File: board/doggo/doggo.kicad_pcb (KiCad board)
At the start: 2 copper layers, 42 x 41.6 mm, 0 parts

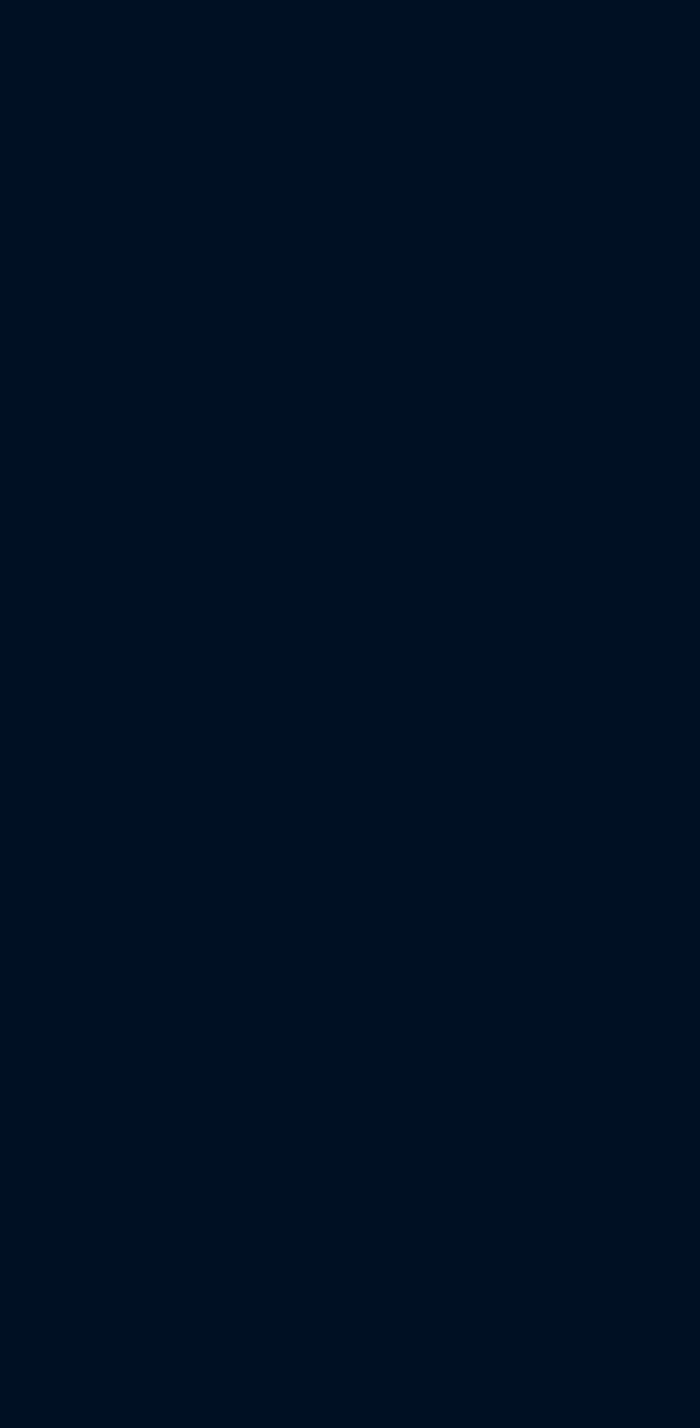
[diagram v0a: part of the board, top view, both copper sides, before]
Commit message: laying out LEDs
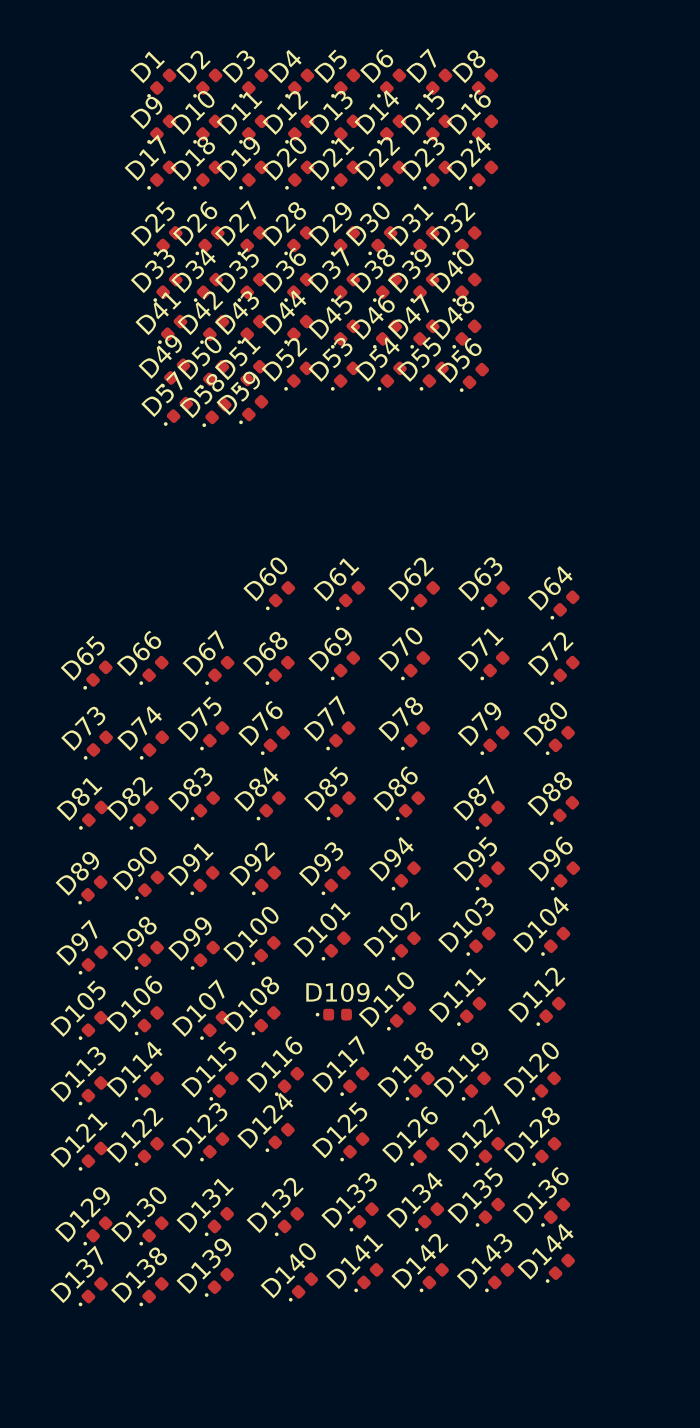
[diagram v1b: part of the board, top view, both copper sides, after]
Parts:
- added D1: LED, Diode_SMD:D_0402_1005Metric, F.Cu at (37.0, 59.0)
- added D10: LED, Diode_SMD:D_0402_1005Metric, F.Cu at (39.5, 61.5)
- added D100: LED, Diode_SMD:D_0402_1005Metric, F.Cu at (42.7, 106.2)
- added D101: LED, Diode_SMD:D_0402_1005Metric, F.Cu at (46.5, 105.9)
- added D102: LED, Diode_SMD:D_0402_1005Metric, F.Cu at (50.3, 105.9)
- added D103: LED, Diode_SMD:D_0402_1005Metric, F.Cu at (54.4, 105.7)
- added D104: LED, Diode_SMD:D_0402_1005Metric, F.Cu at (58.4, 105.7)
- added D105: LED, Diode_SMD:D_0402_1005Metric, F.Cu at (33.3, 110.2)
- added D106: LED, Diode_SMD:D_0402_1005Metric, F.Cu at (36.3, 110.0)
- added D107: LED, Diode_SMD:D_0402_1005Metric, F.Cu at (39.9, 110.2)
- added D108: LED, Diode_SMD:D_0402_1005Metric, F.Cu at (42.7, 110.0)
- added D109: LED, Diode_SMD:D_0402_1005Metric, F.Cu at (46.5, 109.7)
- added D11: LED, Diode_SMD:D_0402_1005Metric, F.Cu at (42.0, 61.5)
- added D110: LED, Diode_SMD:D_0402_1005Metric, F.Cu at (50.0, 109.7)
- added D111: LED, Diode_SMD:D_0402_1005Metric, F.Cu at (53.8, 109.5)
- added D112: LED, Diode_SMD:D_0402_1005Metric, F.Cu at (58.2, 109.5)
- added D113: LED, Diode_SMD:D_0402_1005Metric, F.Cu at (33.3, 113.8)
- added D114: LED, Diode_SMD:D_0402_1005Metric, F.Cu at (36.3, 113.5)
- added D115: LED, Diode_SMD:D_0402_1005Metric, F.Cu at (40.4, 113.5)
- added D116: LED, Diode_SMD:D_0402_1005Metric, F.Cu at (43.9, 113.3)
- added D117: LED, Diode_SMD:D_0402_1005Metric, F.Cu at (47.5, 113.3)
- added D118: LED, Diode_SMD:D_0402_1005Metric, F.Cu at (51.1, 113.5)
- added D119: LED, Diode_SMD:D_0402_1005Metric, F.Cu at (54.1, 113.5)
- added D12: LED, Diode_SMD:D_0402_1005Metric, F.Cu at (44.5, 61.5)
- added D120: LED, Diode_SMD:D_0402_1005Metric, F.Cu at (57.9, 113.5)
- added D121: LED, Diode_SMD:D_0402_1005Metric, F.Cu at (33.3, 117.3)
- added D122: LED, Diode_SMD:D_0402_1005Metric, F.Cu at (36.3, 117.1)
- added D123: LED, Diode_SMD:D_0402_1005Metric, F.Cu at (39.9, 116.8)
- added D124: LED, Diode_SMD:D_0402_1005Metric, F.Cu at (43.4, 116.3)
- added D125: LED, Diode_SMD:D_0402_1005Metric, F.Cu at (47.5, 116.8)
- added D126: LED, Diode_SMD:D_0402_1005Metric, F.Cu at (51.3, 117.1)
- added D127: LED, Diode_SMD:D_0402_1005Metric, F.Cu at (54.9, 117.1)
- added D128: LED, Diode_SMD:D_0402_1005Metric, F.Cu at (57.9, 117.1)
- added D129: LED, Diode_SMD:D_0402_1005Metric, F.Cu at (33.5, 121.4)
- added D13: LED, Diode_SMD:D_0402_1005Metric, F.Cu at (47.0, 61.5)
- added D130: LED, Diode_SMD:D_0402_1005Metric, F.Cu at (36.6, 121.4)
- added D131: LED, Diode_SMD:D_0402_1005Metric, F.Cu at (40.1, 120.9)
- added D132: LED, Diode_SMD:D_0402_1005Metric, F.Cu at (43.9, 120.9)
- added D133: LED, Diode_SMD:D_0402_1005Metric, F.Cu at (48.0, 120.7)
- added D134: LED, Diode_SMD:D_0402_1005Metric, F.Cu at (51.6, 120.7)
- added D135: LED, Diode_SMD:D_0402_1005Metric, F.Cu at (54.9, 120.4)
- added D136: LED, Diode_SMD:D_0402_1005Metric, F.Cu at (58.4, 120.4)
- added D137: LED, Diode_SMD:D_0402_1005Metric, F.Cu at (33.3, 124.7)
- added D138: LED, Diode_SMD:D_0402_1005Metric, F.Cu at (36.6, 124.7)
- added D139: LED, Diode_SMD:D_0402_1005Metric, F.Cu at (40.1, 124.2)
- added D14: LED, Diode_SMD:D_0402_1005Metric, F.Cu at (49.5, 61.5)
- added D140: LED, Diode_SMD:D_0402_1005Metric, F.Cu at (44.7, 124.5)
- added D141: LED, Diode_SMD:D_0402_1005Metric, F.Cu at (48.3, 124.0)
- added D142: LED, Diode_SMD:D_0402_1005Metric, F.Cu at (51.8, 124.0)
- added D143: LED, Diode_SMD:D_0402_1005Metric, F.Cu at (55.4, 124.0)
- added D144: LED, Diode_SMD:D_0402_1005Metric, F.Cu at (58.7, 123.4)
- added D15: LED, Diode_SMD:D_0402_1005Metric, F.Cu at (52.0, 61.5)
- added D16: LED, Diode_SMD:D_0402_1005Metric, F.Cu at (54.5, 61.5)
- added D17: LED, Diode_SMD:D_0402_1005Metric, F.Cu at (37.0, 64.0)
- added D18: LED, Diode_SMD:D_0402_1005Metric, F.Cu at (39.5, 64.0)
- added D19: LED, Diode_SMD:D_0402_1005Metric, F.Cu at (42.0, 64.0)
- added D2: LED, Diode_SMD:D_0402_1005Metric, F.Cu at (39.5, 59.0)
- added D20: LED, Diode_SMD:D_0402_1005Metric, F.Cu at (44.5, 64.0)
- added D21: LED, Diode_SMD:D_0402_1005Metric, F.Cu at (47.0, 64.0)
- added D22: LED, Diode_SMD:D_0402_1005Metric, F.Cu at (49.5, 64.0)
- added D23: LED, Diode_SMD:D_0402_1005Metric, F.Cu at (52.0, 64.0)
- added D24: LED, Diode_SMD:D_0402_1005Metric, F.Cu at (54.5, 64.0)
- added D25: LED, Diode_SMD:D_0402_1005Metric, F.Cu at (37.3, 67.6)
- added D26: LED, Diode_SMD:D_0402_1005Metric, F.Cu at (39.6, 67.6)
- added D27: LED, Diode_SMD:D_0402_1005Metric, F.Cu at (41.9, 67.6)
- added D28: LED, Diode_SMD:D_0402_1005Metric, F.Cu at (44.5, 67.6)
- added D29: LED, Diode_SMD:D_0402_1005Metric, F.Cu at (47.0, 67.6)
- added D3: LED, Diode_SMD:D_0402_1005Metric, F.Cu at (42.0, 59.0)
- added D30: LED, Diode_SMD:D_0402_1005Metric, F.Cu at (49.0, 67.6)
- added D31: LED, Diode_SMD:D_0402_1005Metric, F.Cu at (51.3, 67.6)
- added D32: LED, Diode_SMD:D_0402_1005Metric, F.Cu at (53.6, 67.6)
- added D33: LED, Diode_SMD:D_0402_1005Metric, F.Cu at (37.3, 70.1)
- added D34: LED, Diode_SMD:D_0402_1005Metric, F.Cu at (39.5, 70.1)
- added D35: LED, Diode_SMD:D_0402_1005Metric, F.Cu at (41.9, 70.1)
- added D36: LED, Diode_SMD:D_0402_1005Metric, F.Cu at (44.5, 70.1)
- added D37: LED, Diode_SMD:D_0402_1005Metric, F.Cu at (47.0, 70.1)
- added D38: LED, Diode_SMD:D_0402_1005Metric, F.Cu at (49.3, 70.1)
- added D39: LED, Diode_SMD:D_0402_1005Metric, F.Cu at (51.3, 70.1)
- added D4: LED, Diode_SMD:D_0402_1005Metric, F.Cu at (44.5, 59.0)
- added D40: LED, Diode_SMD:D_0402_1005Metric, F.Cu at (53.6, 70.1)
- added D41: LED, Diode_SMD:D_0402_1005Metric, F.Cu at (37.6, 72.4)
- added D42: LED, Diode_SMD:D_0402_1005Metric, F.Cu at (39.9, 72.4)
- added D43: LED, Diode_SMD:D_0402_1005Metric, F.Cu at (41.9, 72.4)
- added D44: LED, Diode_SMD:D_0402_1005Metric, F.Cu at (44.5, 72.4)
- added D45: LED, Diode_SMD:D_0402_1005Metric, F.Cu at (47.0, 72.6)
- added D46: LED, Diode_SMD:D_0402_1005Metric, F.Cu at (49.3, 72.6)
- added D47: LED, Diode_SMD:D_0402_1005Metric, F.Cu at (51.3, 72.6)
- added D48: LED, Diode_SMD:D_0402_1005Metric, F.Cu at (53.6, 72.6)
- added D49: LED, Diode_SMD:D_0402_1005Metric, F.Cu at (37.8, 74.8)
- added D5: LED, Diode_SMD:D_0402_1005Metric, F.Cu at (47.0, 59.0)
- added D50: LED, Diode_SMD:D_0402_1005Metric, F.Cu at (39.9, 74.8)
- added D51: LED, Diode_SMD:D_0402_1005Metric, F.Cu at (41.9, 74.8)
- added D52: LED, Diode_SMD:D_0402_1005Metric, F.Cu at (44.5, 74.9)
- added D53: LED, Diode_SMD:D_0402_1005Metric, F.Cu at (47.0, 74.9)
- added D54: LED, Diode_SMD:D_0402_1005Metric, F.Cu at (49.5, 74.9)
- added D55: LED, Diode_SMD:D_0402_1005Metric, F.Cu at (51.8, 74.9)
- added D56: LED, Diode_SMD:D_0402_1005Metric, F.Cu at (54.0, 75.0)
- added D57: LED, Diode_SMD:D_0402_1005Metric, F.Cu at (37.9, 76.8)
- added D58: LED, Diode_SMD:D_0402_1005Metric, F.Cu at (40.0, 76.9)
- added D59: LED, Diode_SMD:D_0402_1005Metric, F.Cu at (42.0, 76.8)
- added D6: LED, Diode_SMD:D_0402_1005Metric, F.Cu at (49.5, 59.0)
- added D60: LED, Diode_SMD:D_0402_1005Metric, F.Cu at (43.5, 86.9)
- added D61: LED, Diode_SMD:D_0402_1005Metric, F.Cu at (47.3, 86.9)
- added D62: LED, Diode_SMD:D_0402_1005Metric, F.Cu at (51.3, 86.9)
- added D63: LED, Diode_SMD:D_0402_1005Metric, F.Cu at (55.1, 86.9)
- added D64: LED, Diode_SMD:D_0402_1005Metric, F.Cu at (58.9, 87.4)
- added D65: LED, Diode_SMD:D_0402_1005Metric, F.Cu at (33.5, 91.2)
- added D66: LED, Diode_SMD:D_0402_1005Metric, F.Cu at (36.6, 90.9)
- added D67: LED, Diode_SMD:D_0402_1005Metric, F.Cu at (40.2, 90.9)
- added D68: LED, Diode_SMD:D_0402_1005Metric, F.Cu at (43.4, 90.9)
- added D69: LED, Diode_SMD:D_0402_1005Metric, F.Cu at (47.0, 90.7)
- added D7: LED, Diode_SMD:D_0402_1005Metric, F.Cu at (52.0, 59.0)
- added D70: LED, Diode_SMD:D_0402_1005Metric, F.Cu at (50.8, 90.7)
- added D71: LED, Diode_SMD:D_0402_1005Metric, F.Cu at (55.1, 90.7)
- added D72: LED, Diode_SMD:D_0402_1005Metric, F.Cu at (58.9, 90.9)
- added D73: LED, Diode_SMD:D_0402_1005Metric, F.Cu at (33.6, 95.0)
- added D74: LED, Diode_SMD:D_0402_1005Metric, F.Cu at (36.6, 95.0)
- added D75: LED, Diode_SMD:D_0402_1005Metric, F.Cu at (39.9, 94.5)
- added D76: LED, Diode_SMD:D_0402_1005Metric, F.Cu at (43.2, 94.7)
- added D77: LED, Diode_SMD:D_0402_1005Metric, F.Cu at (46.7, 94.5)
- added D78: LED, Diode_SMD:D_0402_1005Metric, F.Cu at (50.8, 94.5)
- added D79: LED, Diode_SMD:D_0402_1005Metric, F.Cu at (55.1, 94.7)
- added D8: LED, Diode_SMD:D_0402_1005Metric, F.Cu at (54.5, 59.0)
- added D80: LED, Diode_SMD:D_0402_1005Metric, F.Cu at (58.7, 94.7)
- added D81: LED, Diode_SMD:D_0402_1005Metric, F.Cu at (33.3, 98.8)
- added D82: LED, Diode_SMD:D_0402_1005Metric, F.Cu at (36.0, 98.8)
- added D83: LED, Diode_SMD:D_0402_1005Metric, F.Cu at (39.4, 98.3)
- added D84: LED, Diode_SMD:D_0402_1005Metric, F.Cu at (42.9, 98.3)
- added D85: LED, Diode_SMD:D_0402_1005Metric, F.Cu at (46.8, 98.3)
- added D86: LED, Diode_SMD:D_0402_1005Metric, F.Cu at (50.5, 98.3)
- added D87: LED, Diode_SMD:D_0402_1005Metric, F.Cu at (54.9, 98.8)
- added D88: LED, Diode_SMD:D_0402_1005Metric, F.Cu at (58.9, 98.6)
- added D89: LED, Diode_SMD:D_0402_1005Metric, F.Cu at (33.3, 102.9)
- added D9: LED, Diode_SMD:D_0402_1005Metric, F.Cu at (37.0, 61.5)
- added D90: LED, Diode_SMD:D_0402_1005Metric, F.Cu at (36.3, 102.6)
- added D91: LED, Diode_SMD:D_0402_1005Metric, F.Cu at (39.3, 102.4)
- added D92: LED, Diode_SMD:D_0402_1005Metric, F.Cu at (42.7, 102.4)
- added D93: LED, Diode_SMD:D_0402_1005Metric, F.Cu at (46.5, 102.4)
- added D94: LED, Diode_SMD:D_0402_1005Metric, F.Cu at (50.3, 102.1)
- added D95: LED, Diode_SMD:D_0402_1005Metric, F.Cu at (54.9, 102.1)
- added D96: LED, Diode_SMD:D_0402_1005Metric, F.Cu at (59.0, 102.1)
- added D97: LED, Diode_SMD:D_0402_1005Metric, F.Cu at (33.3, 106.7)
- added D98: LED, Diode_SMD:D_0402_1005Metric, F.Cu at (36.3, 106.4)
- added D99: LED, Diode_SMD:D_0402_1005Metric, F.Cu at (39.4, 106.4)

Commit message: finally got the FUCKING svg2shenzen to barely work enough so I could hack together a footprint
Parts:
- added G***: doggo_accents, doggo:doggo_accents, F.Cu at (136.0, 93.3)
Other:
- board size 42 x 41.6 mm -> 98.1 x 97.5 mm

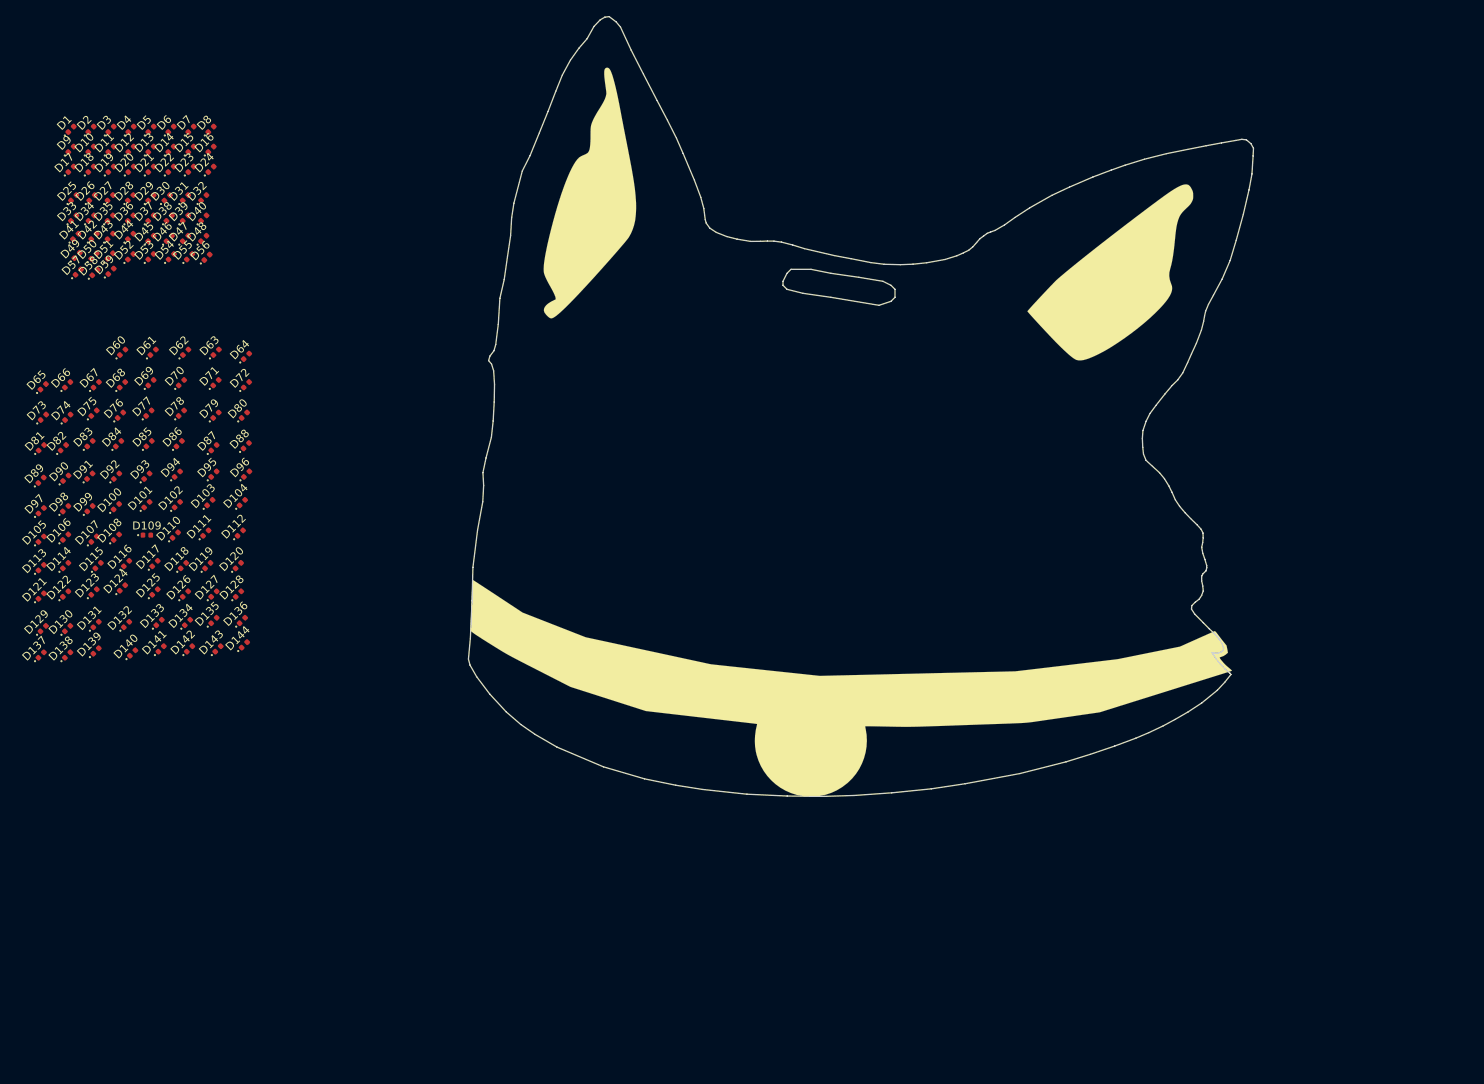
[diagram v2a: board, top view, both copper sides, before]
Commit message: worked on power support, layed out LED array
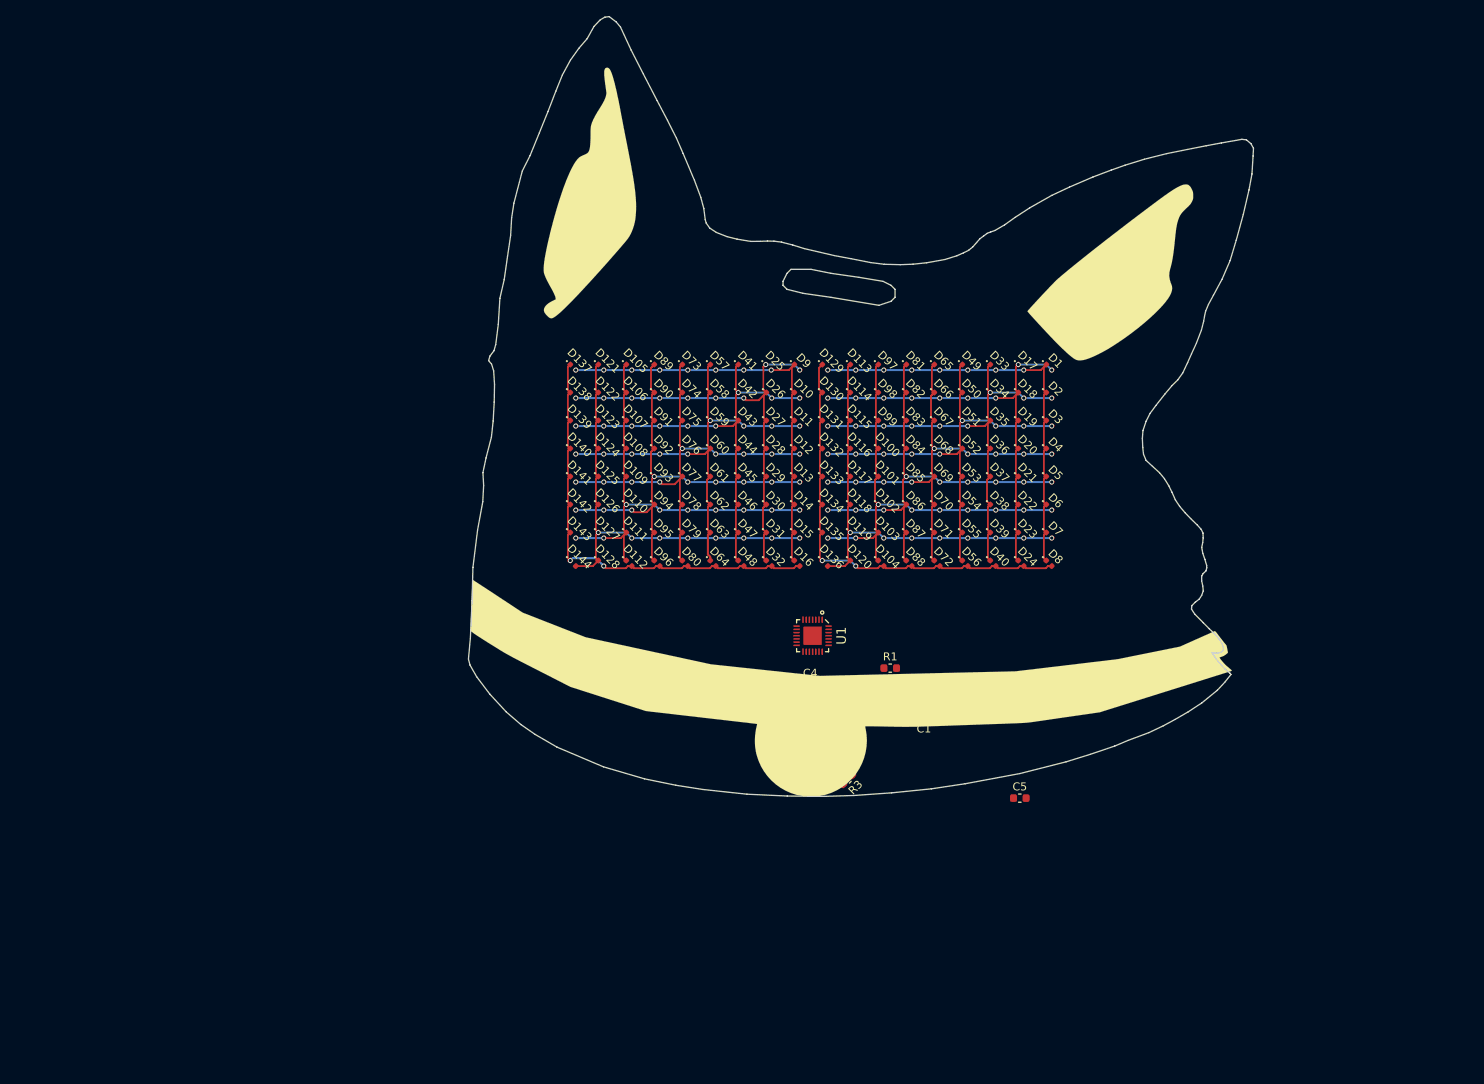
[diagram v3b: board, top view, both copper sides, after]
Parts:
- added C1: 100nF, Capacitor_SMD:C_0603_1608Metric, F.Cu at (143.6, 132.5)
- added C2: 1uF, Capacitor_SMD:C_0805_2012Metric, F.Cu at (150.8, 129.8)
- added C3: 100nF, Capacitor_SMD:C_0603_1608Metric, F.Cu at (152.8, 129.8)
- added C4: 100nF, Capacitor_SMD:C_0603_1608Metric, F.Cu at (129.4, 128.4)
- added C5: 220nF, Capacitor_SMD:C_0603_1608Metric, F.Cu at (155.6, 142.6)
- added C6: 100nF, Capacitor_SMD:C_0603_1608Metric, F.Cu at (144.1, 128.9)
- added R1: 4.7k, Resistor_SMD:R_0603_1608Metric, F.Cu at (139.4, 126.3)
- added R2: 4.7k, Resistor_SMD:R_0603_1608Metric, F.Cu at (133.4, 130.3)
- added R3: 4.7k, Resistor_SMD:R_0603_1608Metric, F.Cu at (134.1, 140.2)
- added R32: 1k, Resistor_SMD:R_0603_1608Metric, F.Cu at (113.8, 130.2)
- added R33: 1k, Resistor_SMD:R_0603_1608Metric, F.Cu at (113.8, 128.5)
- added R4: 100k, Resistor_SMD:R_0603_1608Metric, F.Cu at (146.2, 128.9)
- added R5: 100k, Resistor_SMD:R_0603_1608Metric, F.Cu at (146.2, 131.9)
- added R6: 1k, Resistor_SMD:R_0603_1608Metric, F.Cu at (124.5, 130.2)
- added R7: 536K, Resistor_SMD:R_0603_1608Metric, F.Cu at (107.2, 125.9)
- added R8: 309K, Resistor_SMD:R_0603_1608Metric, F.Cu at (106.4, 128.2)
- added U1: IS31FL3731, doggo:IS31FL3731, F.Cu at (129.7, 122.3)
- added U2: LIS2HH12, doggo:LIS2HH12, F.Cu at (117.2, 128.8)
- added U3: STM32F042K6, Package_QFP:LQFP-32_7x7mm_P0.8mm, F.Cu at (129.5, 135.8)
- added U4: MCP1640, Package_TO_SOT_SMD:SOT-23-6, F.Cu at (102.5, 126.5)
- moved D1 125.8 mm to (159.2, 88.8), turned to 315 degrees
- moved D2 124.3 mm to (159.2, 92.2), turned to 315 degrees
- moved D3 122.9 mm to (159.2, 95.8), turned to 315 degrees
- moved D4 121.6 mm to (159.2, 99.2), turned to 315 degrees
- moved D17 121.3 mm to (155.8, 88.8), turned to 315 degrees
- moved D5 120.5 mm to (159.2, 102.8), turned to 315 degrees
- moved D18 119.6 mm to (155.8, 92.2), turned to 315 degrees
- moved D6 119.5 mm to (159.2, 106.2), turned to 315 degrees
- moved D7 118.7 mm to (159.2, 109.8), turned to 315 degrees
- moved D19 118.1 mm to (155.8, 95.8), turned to 315 degrees
- moved D8 118.0 mm to (159.2, 113.2), turned to 315 degrees
- moved D20 116.7 mm to (155.8, 99.2), turned to 315 degrees
- moved D33 116.4 mm to (152.2, 88.8), turned to 315 degrees
- moved D21 115.4 mm to (155.8, 102.8), turned to 315 degrees
- moved D34 114.9 mm to (152.2, 92.2), turned to 315 degrees
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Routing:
- net /CB9: track 0.00 -> 57.1 mm, vias 0 -> 2
- net /CA9: track 0.00 -> 56.9 mm, vias 0 -> 2
- net /CB4: track 0.00 -> 54.9 mm, vias 0 -> 9
- net /CA3: track 0.00 -> 54.9 mm, vias 0 -> 9
- net /CA7: track 0.00 -> 54.9 mm, vias 0 -> 9
- net /CA5: track 0.00 -> 54.9 mm, vias 0 -> 9
- net /CA6: track 0.00 -> 54.9 mm, vias 0 -> 9
- net /CB7: track 0.00 -> 54.8 mm, vias 0 -> 9
- net /CA4: track 0.00 -> 54.8 mm, vias 0 -> 9
- net /CA8: track 0.00 -> 54.8 mm, vias 0 -> 8
- net /CB3: track 0.00 -> 54.8 mm, vias 0 -> 9
- net /CA2: track 0.00 -> 54.8 mm, vias 0 -> 9
- net /CB8: track 0.00 -> 54.8 mm, vias 0 -> 8
- net /CB6: track 0.00 -> 54.8 mm, vias 0 -> 9
- net /CB2: track 0.00 -> 54.8 mm, vias 0 -> 9
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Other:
- outline, holes or cut-outs redrawn
